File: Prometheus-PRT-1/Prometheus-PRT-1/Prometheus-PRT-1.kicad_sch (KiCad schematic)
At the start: 16 parts, among them J1 Conn_02x10, J2 AppleIIBus, U1 74LS74, U2 74LS74, U3 74LS00, U4 74LS374, U5 74LS30, U6 74LS08, U7 MM27C16Q-1, U8 74LS08, U9 74LS00

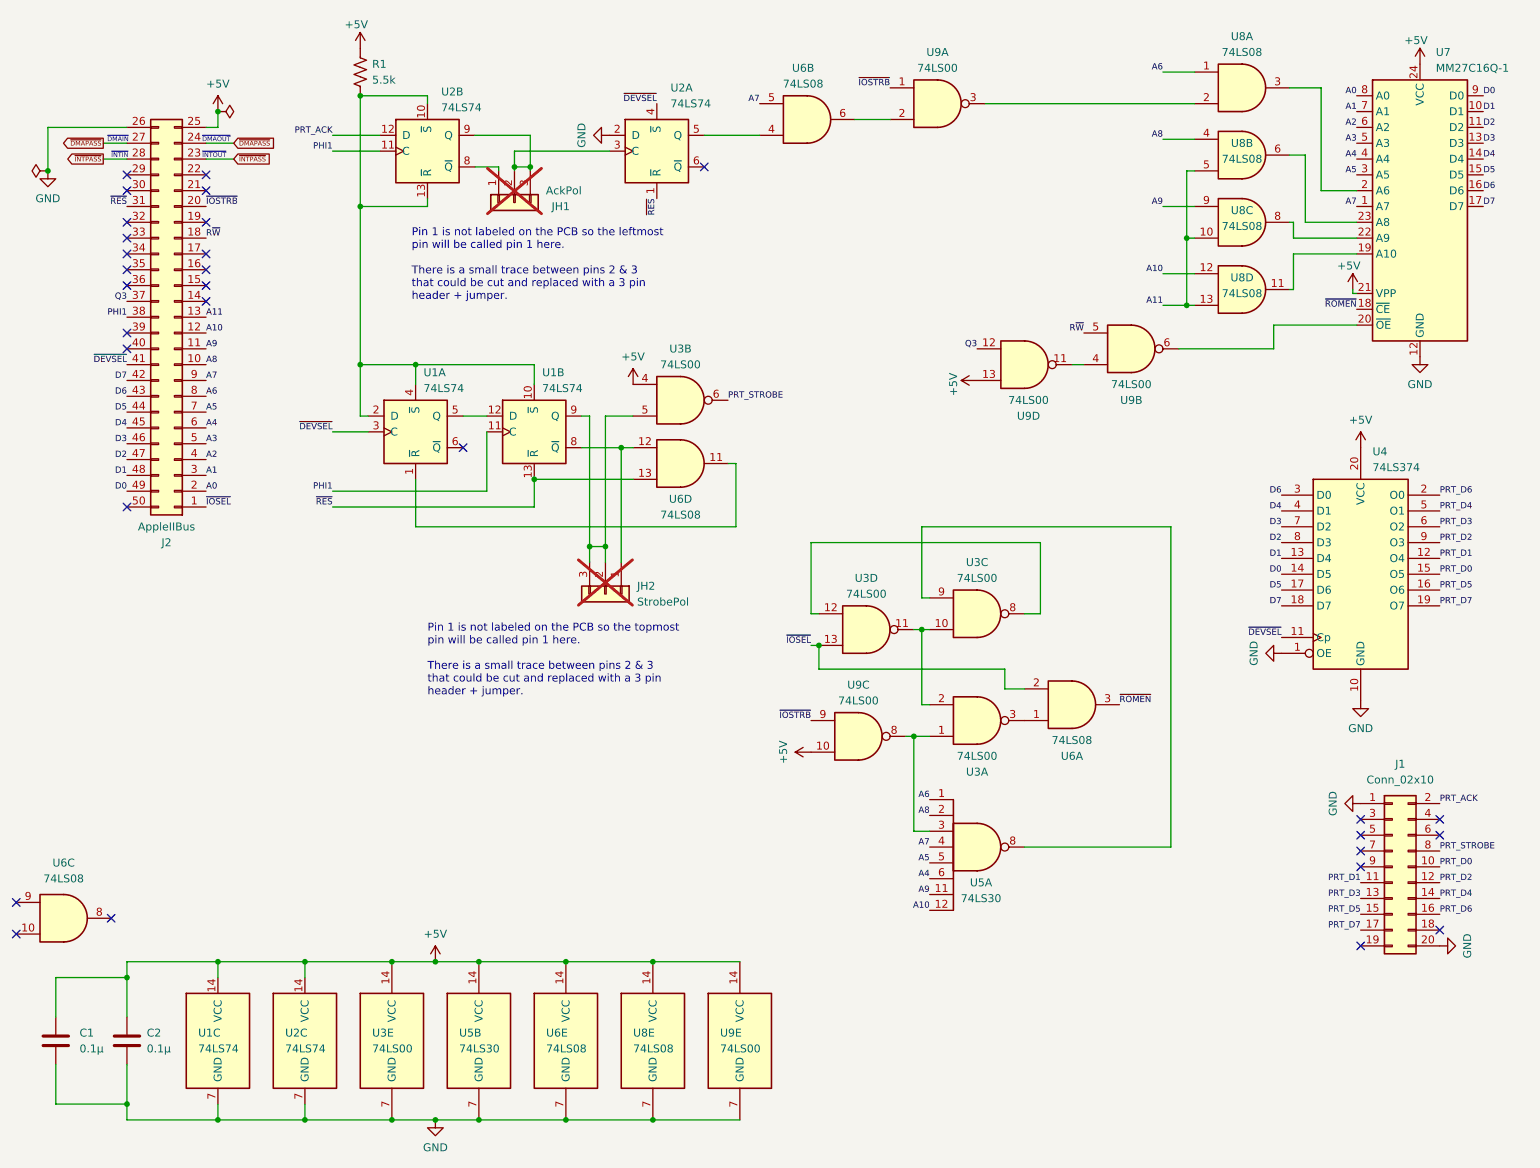
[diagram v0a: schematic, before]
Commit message: Update Prometheus-PRT-1 to kicad8 and the shared symbol library
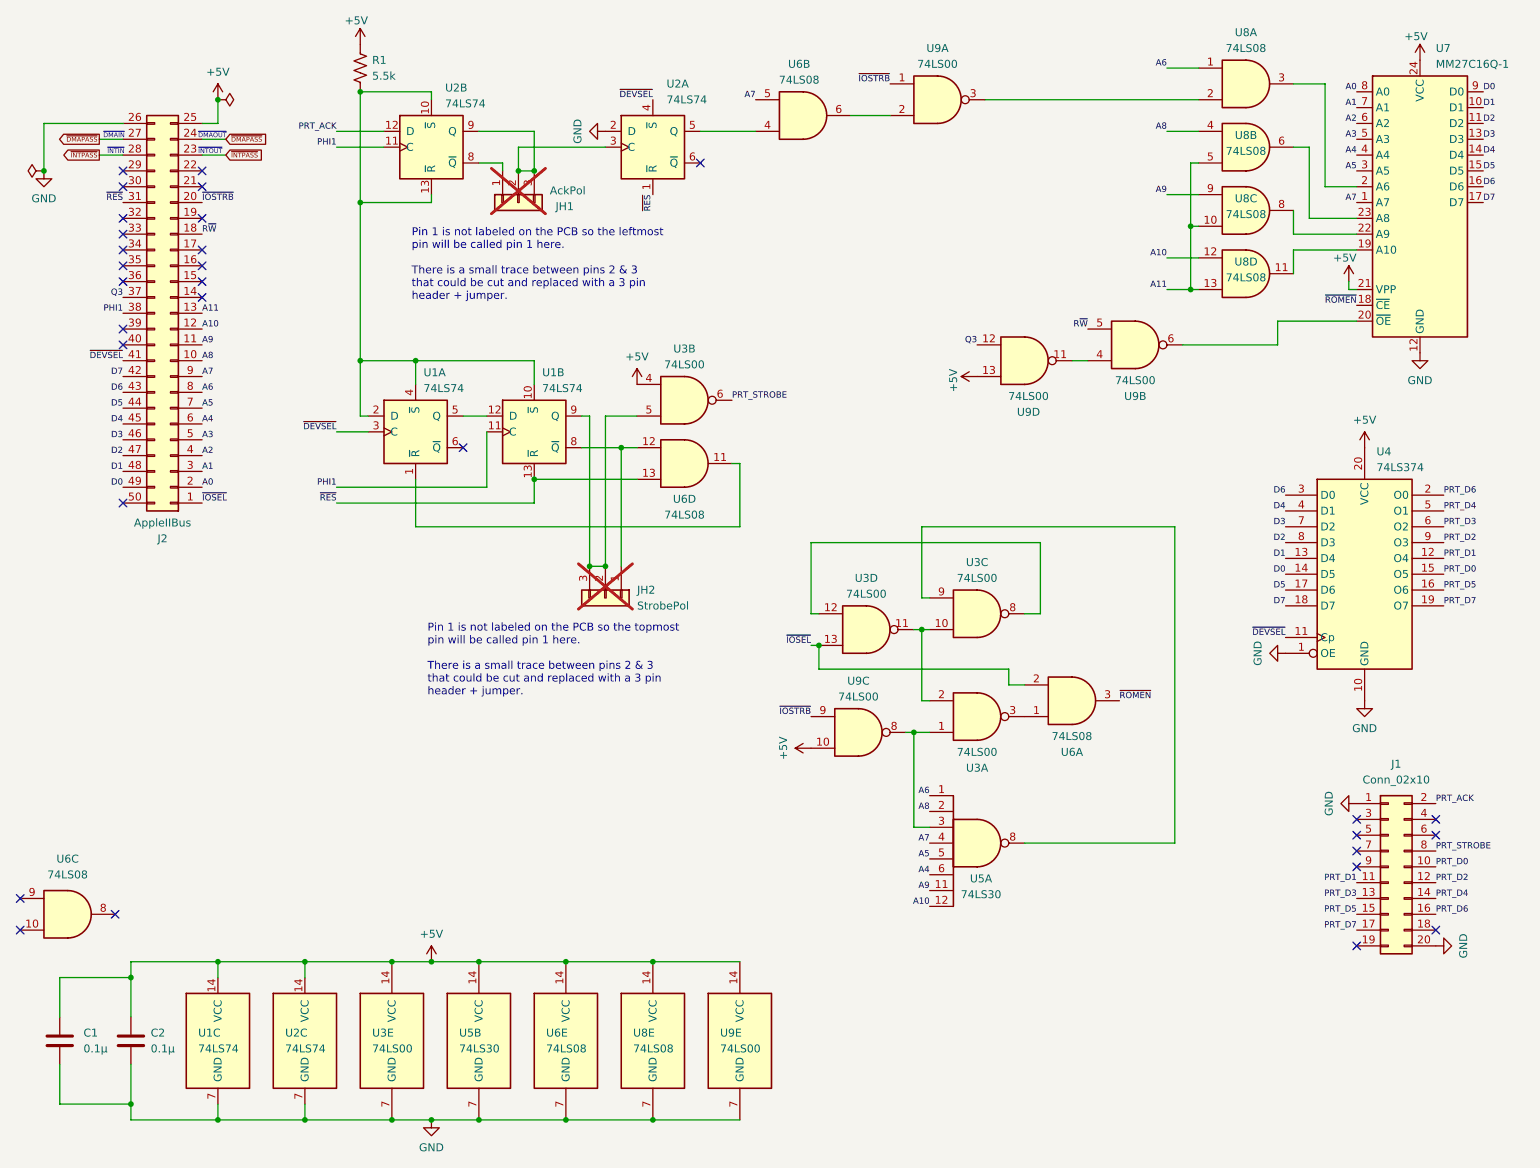
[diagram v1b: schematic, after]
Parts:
- J2: footprint Apple:AppleIIBus_Edge -> (none)
- U7: symbol Memory:27C16 -> Memory_Legacy:27C16
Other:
- moved on the sheet: C1, C2, J1, J2, JH1, JH2, R1, U2A, U2B, U3A, U3B, U4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
